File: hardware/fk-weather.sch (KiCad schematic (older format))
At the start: 77 parts, among them J1 MICRO-USB, J2 CONN_01X03, J6 CONN-HDR-2x5, M1 MOUNT_HOLE, M2 MOUNT_HOLE, M3 MOUNT_HOLE, M4 MOUNT_HOLE, P101 CONN_01X05, Q1 2N7002LT1G, Q2 2N7002LT1G, Q3 2N7002LT1G, SW1 SPNO, U1 ATSAMD21G18A-AU, U101 TSL2591, U102 MPL3115A2, U103 BNO055, U104 SHT31, U2 MCP1700T-XXX2E, U3 MAX4466, Y1 FC-135, Y101 FC-135

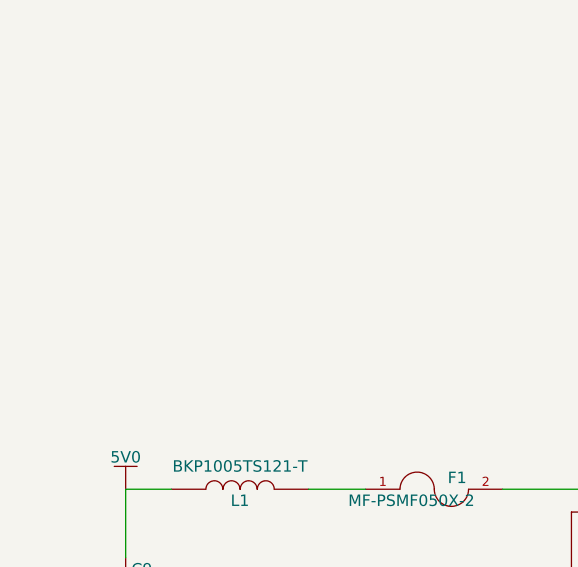
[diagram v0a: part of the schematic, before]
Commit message: Working on layout issues, trying to figure out the MCU problem.
Also broke up power from USB.
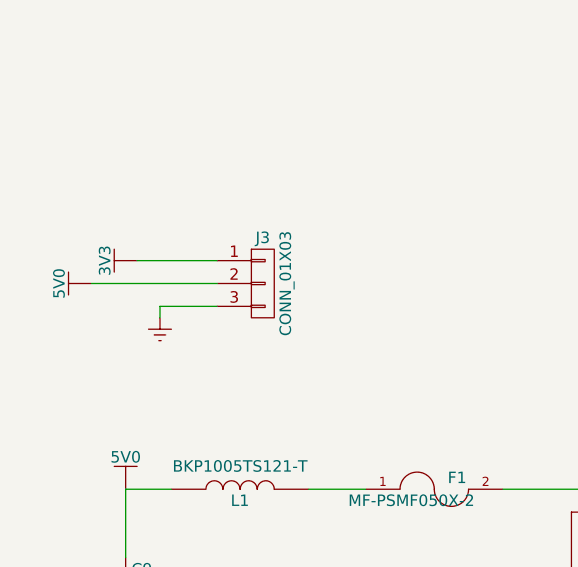
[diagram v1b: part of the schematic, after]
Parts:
- added J3: CONN_01X03, Socket_Strips:Socket_Strip_Straight_1x03_Pitch2.54mm, symbol CONN_01X03
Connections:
- wire segments 256 -> 260
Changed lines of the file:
@@
 NoConn ~ 5050 9900
 NoConn ~ 5050 10000
+$Comp
+L CONN_01X03 J3
+U 1 1 599F8F90
+P 1850 8550
+F 0 "J3" H 1850 8750 50  0000 C CNN
+F 1 "CONN_01X03" V 1950 8550 50  0000 C CNN
+F 2 "Socket_Strips:Socket_Strip_Straight_1x03_Pitch2.54mm" H 1850 8550 50  0001 C CNN
+F 3 "" H 1850 8550 50  0001 C CNN
+	1    1850 8550
+	1    0    0    -1
+$EndComp
+$Comp
+L 5V0 #PWR058
+U 1 1 599F9AB2
+P 1100 8550
+F 0 "#PWR058" H 1100 8400 50  0001 C CNN
+F 1 "5V0" H 1100 8690 50  0000 C CNN
+F 2 "" H 1100 8550 60  0000 C CNN
+F 3 "" H 1100 8550 60  0000 C CNN
+	1    1100 8550
+	0    -1   -1   0
+$EndComp
+$Comp
+L 3V3 #PWR059
+U 1 1 599FA087
+P 1300 8450
+F 0 "#PWR059" H 1300 8300 50  0001 C CNN
+F 1 "3V3" H 1300 8590 50  0000 C CNN
+F 2 "" H 1300 8450 60  0000 C CNN
+F 3 "" H 1300 8450 60  0000 C CNN
+	1    1300 8450
+	0    -1   -1   0
+$EndComp
+$Comp
+L GND #PWR060
+U 1 1 599FA572
+P 1400 8700
+F 0 "#PWR060" H 1400 8450 50  0001 C CNN
+F 1 "GND" H 1400 8550 50  0001 C CNN
+F 2 "" H 1400 8700 60  0000 C CNN
+F 3 "" H 1400 8700 60  0000 C CNN
+	1    1400 8700
+	1    0    0    -1
+$EndComp
+Wire Wire Line
+	1300 8450 1650 8450
+Wire Wire Line
+	1100 8550 1650 8550
+Wire Wire Line
+	1400 8700 1400 8650
+Wire Wire Line
+	1400 8650 1650 8650
 $EndSCHEMATC

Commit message: Programming header was wrong from the SMD switch.
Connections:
- wire segments 260 -> 259
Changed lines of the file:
@@
 L 3V3 #PWR015
 U 1 1 5611121D
-P 7000 1400
-F 0 "#PWR015" H 7000 1250 50  0001 C CNN
-F 1 "3V3" H 7000 1540 50  0000 C CNN
-F 2 "" H 7000 1400 60  0000 C CNN
-F 3 "" H 7000 1400 60  0000 C CNN
-	1    7000 1400
-	1    0    0    -1
+P 6800 1900
+F 0 "#PWR015" H 6800 1750 50  0001 C CNN
+F 1 "3V3" H 6800 2040 50  0000 C CNN
+F 2 "" H 6800 1900 60  0000 C CNN
+F 3 "" H 6800 1900 60  0000 C CNN
+	1    6800 1900
+	0    -1   -1   0
 $EndComp
 $Comp
 L GND #PWR016
 U 1 1 561119A2
-P 7000 2000
-F 0 "#PWR016" H 7000 1750 50  0001 C CNN
-F 1 "GND" H 7000 1850 50  0001 C CNN
-F 2 "" H 7000 2000 60  0000 C CNN
-F 3 "" H 7000 2000 60  0000 C CNN
-	1    7000 2000
-	1    0    0    -1
+P 7000 1350
+F 0 "#PWR016" H 7000 1100 50  0001 C CNN
+F 1 "GND" H 7000 1200 50  0001 C CNN
+F 2 "" H 7000 1350 60  0000 C CNN
+F 3 "" H 7000 1350 60  0000 C CNN
+	1    7000 1350
+	-1   0    0    1
 $EndComp
 $Comp
@@
 Text Label 4350 1950 0    50   ~ 0
 RESET
-Text Label 7650 1500 0    50   ~ 0
+Text Label 7650 1900 0    50   ~ 0
 SWDIO
-Text Label 7650 1600 0    50   ~ 0
+Text Label 7650 1800 0    50   ~ 0
 SWCLK
-Text Label 7650 1900 0    50   ~ 0
+Text Label 7750 1500 0    50   ~ 0
 RST
 Text Label 3900 1500 0    50   ~ 0
@@
 	1800 2850 1800 2750
 Wire Wire Line
-	7000 1400 7000 1500
-Wire Wire Line
-	7000 1500 7100 1500
-Wire Wire Line
-	7100 1600 7000 1600
-Wire Wire Line
-	7000 1600 7000 2000
-Wire Wire Line
-	7100 1900 7000 1900
-Wire Wire Line
 	7100 1700 7000 1700
 Wire Wire Line
 	7600 1500 7900 1500
-Wire Wire Line
-	7900 1600 7600 1600
 Wire Wire Line
 	7900 1900 7600 1900
@@
 Connection ~ 1950 2250
 Connection ~ 1800 2750
-Connection ~ 7000 1900
 Connection ~ 7000 1700
 Connection ~ 11550 1400
@@
 Connection ~ 11150 7300
 Connection ~ 12500 6650
-NoConn ~ 7100 1800
-NoConn ~ 7600 1700
-NoConn ~ 7600 1800
 NoConn ~ 8850 1500
 NoConn ~ 8850 1400
@@
 Wire Wire Line
 	1400 8650 1650 8650
+Wire Wire Line
+	7900 1800 7600 1800
+NoConn ~ 7600 1700
+NoConn ~ 7600 1600
+NoConn ~ 7100 1600
+Wire Wire Line
+	7000 1800 7100 1800
+Wire Wire Line
+	7000 1350 7000 1800
+Wire Wire Line
+	7000 1500 7100 1500
+Connection ~ 7000 1500
+Wire Wire Line
+	7100 1900 6800 1900
 $EndSCHEMATC

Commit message: Adding an LED to D13
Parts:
- added D5: Orange, RocketScreamKicadLibrary:LED-0603, symbol LED-SINGLE
- added Q4: 2N7002LT1G, RocketScreamKicadLibrary:SOT-23, symbol MOSFET-N
- added R17: 2k2, Resistors_SMD:R_0603_HandSoldering, symbol RESISTOR
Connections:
- net labels added: D13
- wire segments 259 -> 265

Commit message: Removing extraneous headers.
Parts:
- removed J3: CONN_01X03, Socket_Strips:Socket_Strip_Straight_1x03_Pitch2.54mm, symbol CONN_01X03
- removed P101: CONN_01X05, Socket_Strips:Socket_Strip_Straight_1x05_Pitch2.54mm, symbol CONN_01X05
- added J3: CONN_01X06, Socket_Strips:Socket_Strip_Straight_1x06_Pitch2.54mm, symbol CONN_01X06
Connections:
- wire segments 265 -> 262

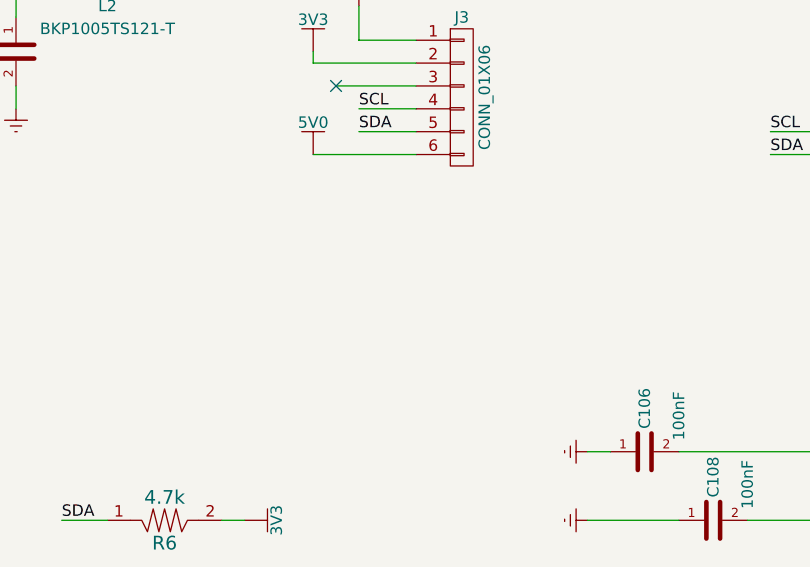
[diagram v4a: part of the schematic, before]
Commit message: Adding a header for an LED.
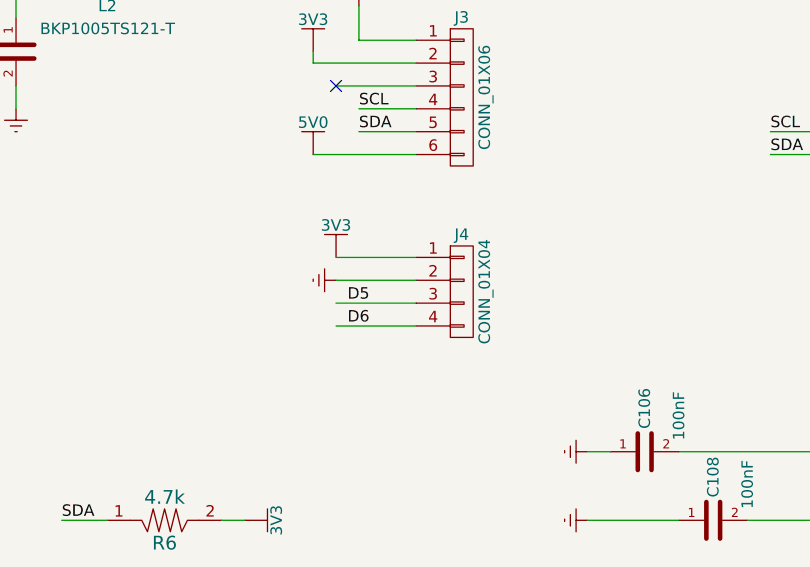
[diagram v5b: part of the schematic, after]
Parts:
- added J4: CONN_01X04, Socket_Strips:Socket_Strip_Straight_1x04_Pitch2.54mm, symbol CONN_01X04
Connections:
- wire segments 262 -> 266

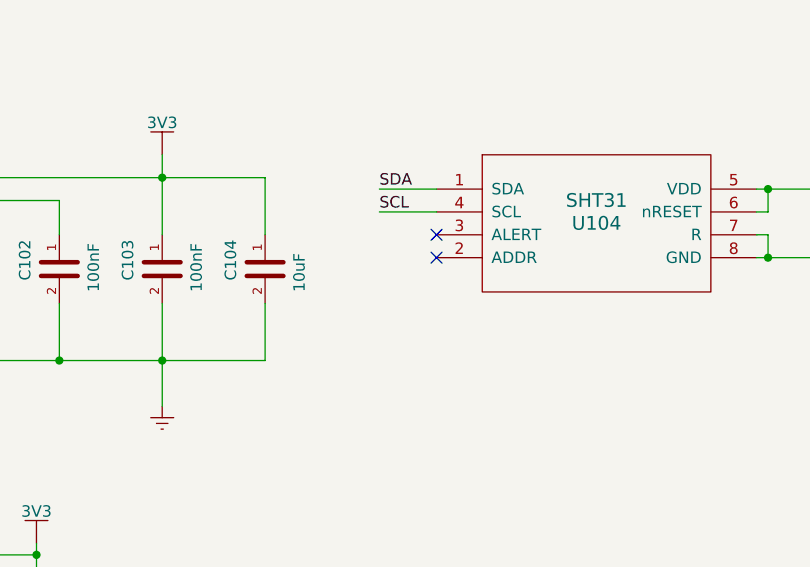
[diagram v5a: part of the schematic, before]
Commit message: Wire ADDR on SHT31 to GND.
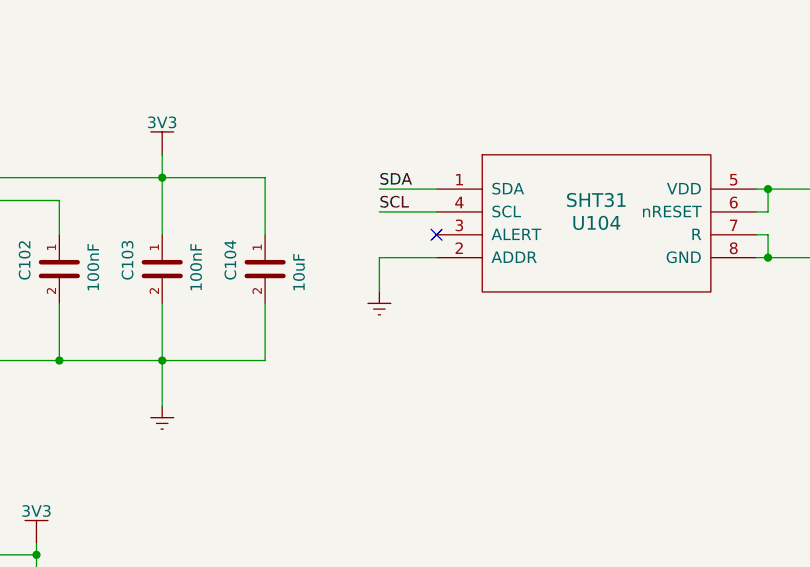
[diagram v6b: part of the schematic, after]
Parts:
- C10: spn1 603-AC603KRX7R8BB472 -> 80-C0603C472K9R
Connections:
- wire segments 266 -> 268
- no-connect marks 16 -> 15

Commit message: Some parts.
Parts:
- C1, C10, C101, C102, C103, C104, C105, C106, C107, C108, C109, C13, C14, C15, C16, C17, C2, C3, C4, C5, C6, C7, C8, C9, D1, D4, D5, F1, J2, J3, J4, J6, L1, L2, L3, L4, M1, M2, M3, M4, MK1, Q1, Q2, Q3, Q4, R1, R10, R101, R102, R103, R11, R12, R13, R14, R15, R16, R17, R2, R3, R4, R5, R8, R9, RV1, U1, U101, U102, U103, U104, U2, U3, Y1, Y101: price (none) -> 0
- C11, C12: price (none) -> 0; spn1 581-0603YD105K -> 963-UMK107BJ105KA-T
- D2: price (none) -> 0; spn1 859-LTST-C190KFKT -> 859-LTST-C190KSKT
- D3: price (none) -> 0; spn1 859-LTST-C190KFKT -> 859-LTST-C191TBKT
- J1: price (none) -> 0; spn1 (none) -> 798-ZX62D-B-5PA830
- R6, R7: value 4.7k -> 4.7K; price (none) -> 0
- SW1: price (none) -> 0; spn1 (none) -> 732-7055-1-ND

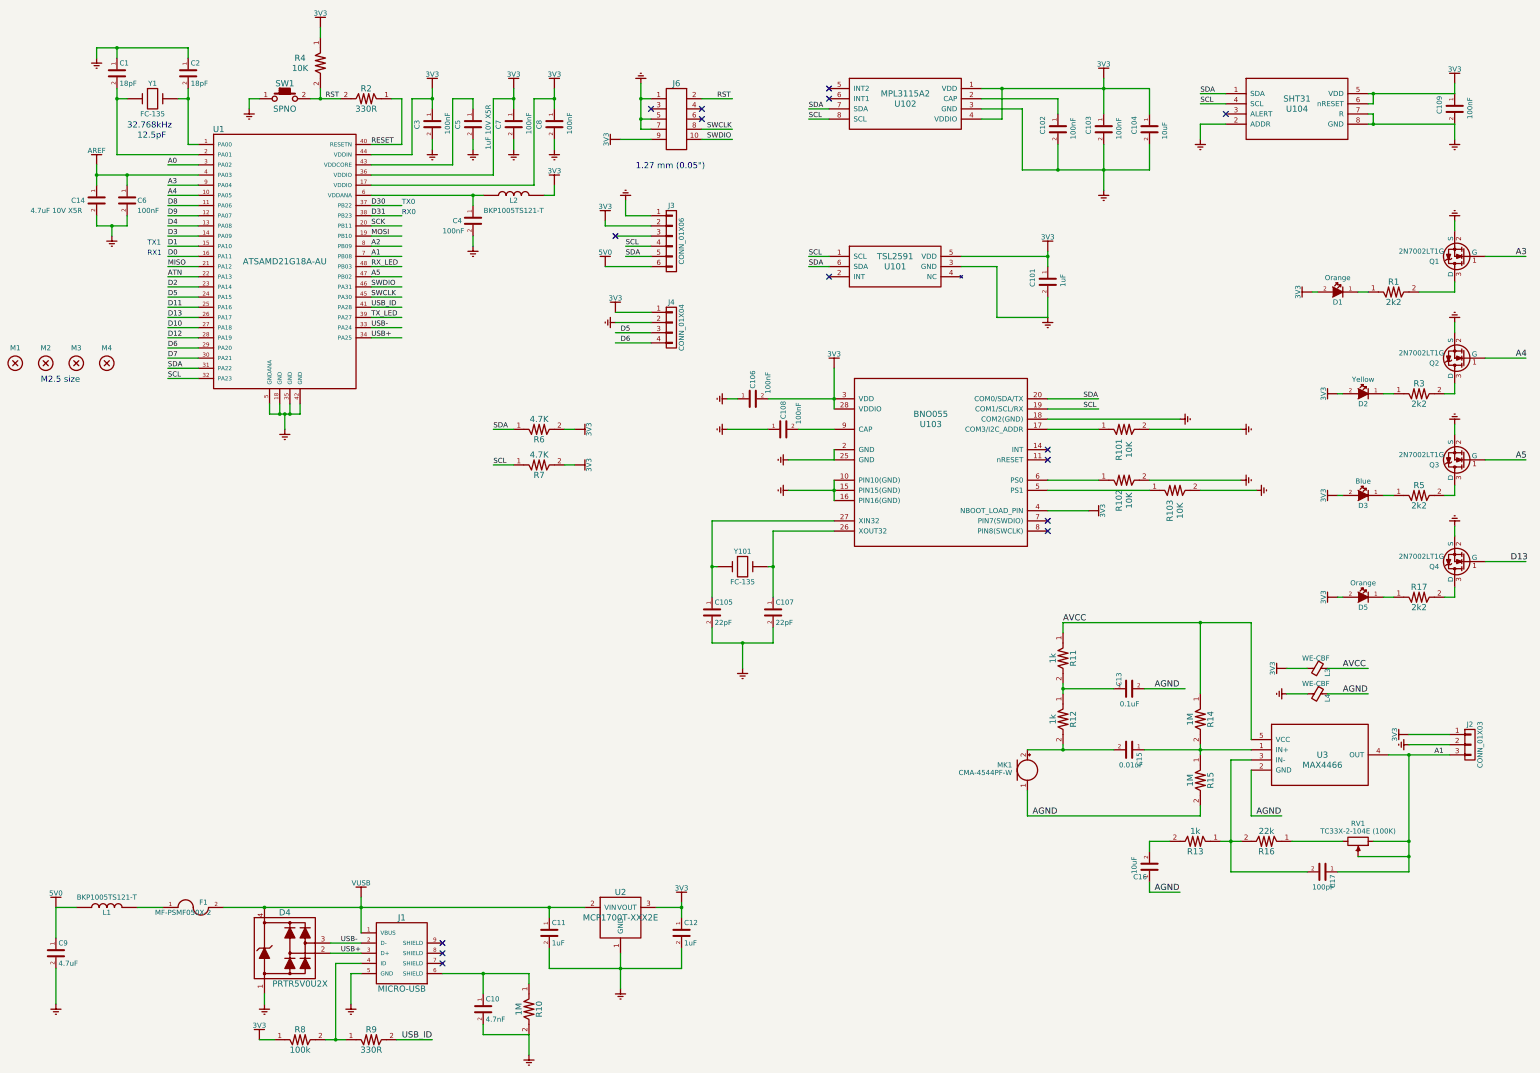
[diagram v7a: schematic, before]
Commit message: Add way to isolate sensors in from the bus in testing.
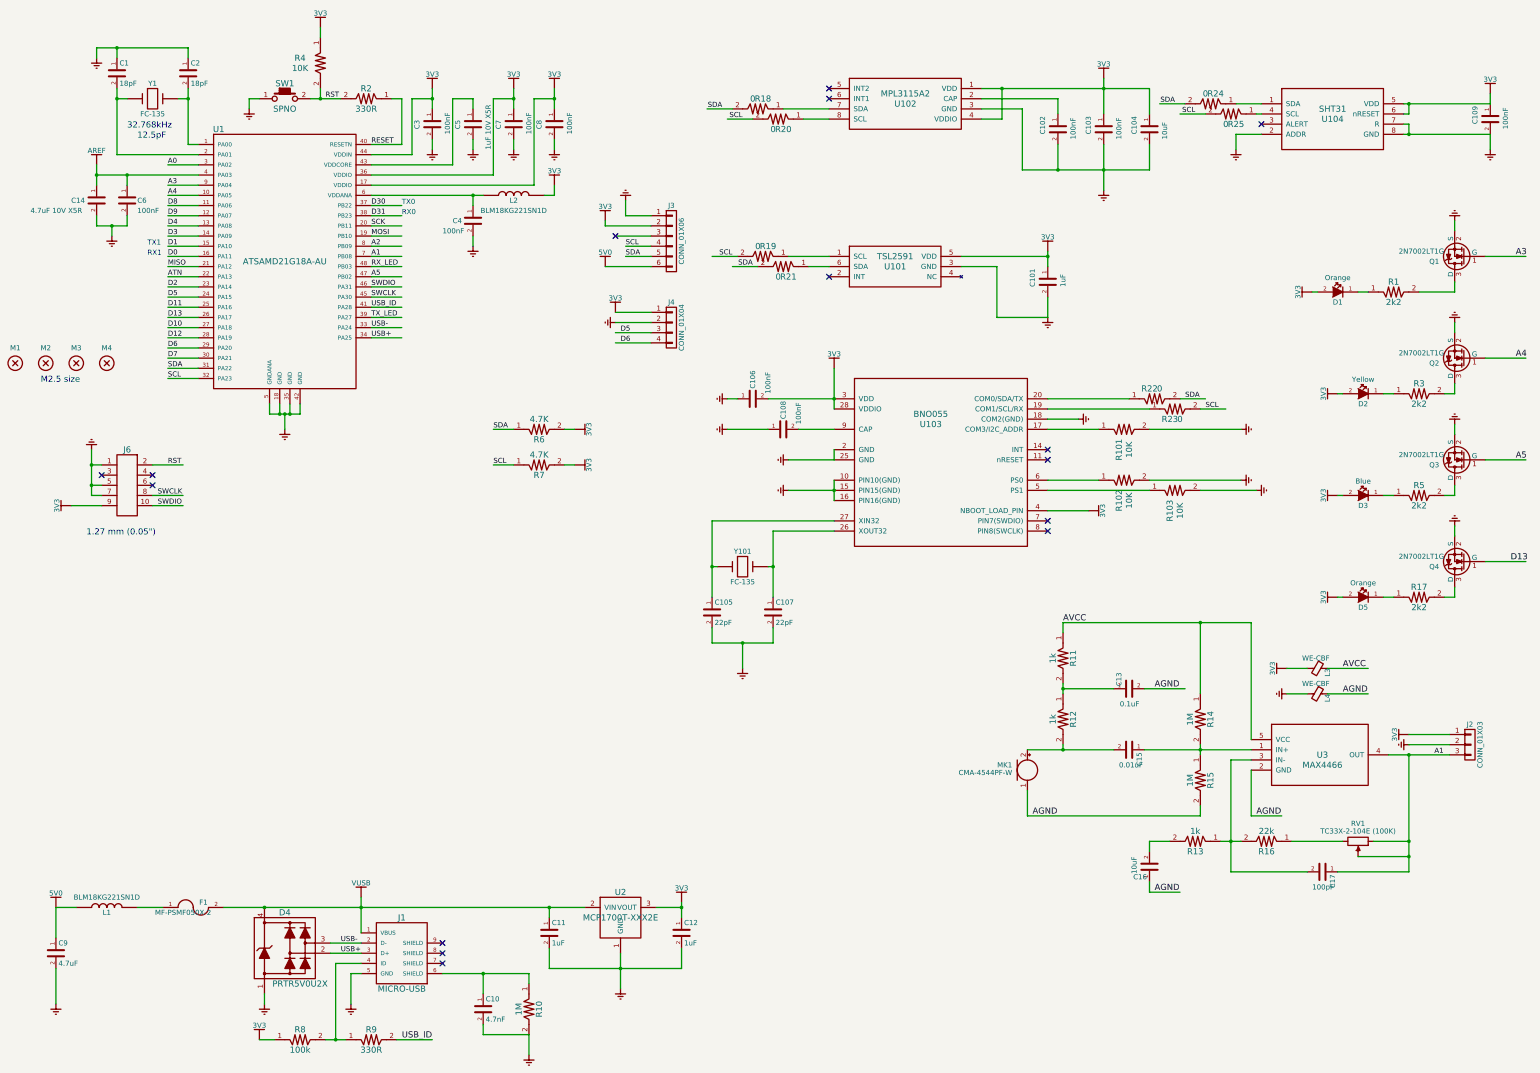
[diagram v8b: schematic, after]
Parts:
- added R18, R19, R20, R21, R22, R23, R24, R25: 0, conservify:SJ_SHORTED, symbol RESISTOR
- L1, L2: value BKP1005TS121-T -> BLM18KG221SN1D; spn1 963-BKP1608HS121-T -> 81-BLM18KG221SN1D
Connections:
- wire segments 268 -> 276
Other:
- moved on the sheet: C109, J6, U104
